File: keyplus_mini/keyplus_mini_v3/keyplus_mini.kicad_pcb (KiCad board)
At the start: 2 copper layers, 24.1 x 23 mm, 23 parts, among them J1 USB_C_Receptacle, J2 Conn_02x09_Odd_Even, J3 CONN_01X01, J4 Conn_02x09_Odd_Even, U1 MCP1700-3302E_SOT23, U2 ATXMEGA-A4U-EPAD

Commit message: cleanup keyplus mini_v3
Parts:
- removed OSHW_Logo: G***, logo:OSHW_3x3mm_SilkS
- added ?: REF**, logo:key+_5mm, F.Cu at (203.2, 114.5)
- added ?: , logo:OSHW_3x3mm_SilkS, B.Cu at (207.1, 112.4)
- C2: footprint Capacitor_SMD:C_1206_3216Metric -> Capacitor_SMD:C_0805_2012Metric
- J1: footprint conn_usb:USB_TypeC_239FC14-00276T-H -> conn_usb:USB_TypeC_Hirose_CX70M-24P1
- moved R3 1.82 mm to (200.8, 98.3)
- moved R1 1.14 mm to (209.6, 102.5), turned to 0 degrees
- moved R5 1.00 mm to (211.8, 102.5)
- moved J1 1.00 mm to (208.0, 92.0)
- moved R4 1.00 mm to (214.1, 102.5)
- moved C2 0.59 mm to (212.7, 104.0)
- moved R2 0.56 mm to (206.3, 102.7), turned to 0 degrees
- moved ? 0.41 mm to (217.1, 95.4)
- moved ? 0.40 mm to (198.9, 95.4)
- moved R6 0.22 mm to (204.9, 102.4)
- moved R7 0.15 mm to (205.3, 103.8)
- moved C1 0.14 mm to (202.8, 105.2)
- moved U1 0.13 mm to (202.3, 102.9)
- moved C5 0.12 mm to (206.8, 104.8)
- moved D1 0.08 mm to (202.4, 107.6)
- renumbered REF** to ?
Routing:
- net +5V: track 16.7 -> 27.3 mm
- net GND: track 25.2 -> 30.4 mm, vias 24 -> 23
- net +3V3: track 82.2 -> 86.3 mm
- net Net-(J1-PadB5): track 2.68 -> 5.51 mm, vias 0 -> 1
- net /PCL: track 16.8 -> 18.6 mm
- net /PE1: track 17.5 -> 19.1 mm
- net /PC2: track 9.31 -> 7.81 mm
- net /D-: track 7.93 -> 9.04 mm, vias 0 -> 1
- net /PA5: track 9.44 -> 10.2 mm
- net Net-(R6-Pad2): track 4.24 -> 4.94 mm
- net /PE0: track 15.6 -> 15.0 mm
- net Net-(C1-Pad2): track 2.61 -> 3.13 mm
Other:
- board size 24.1 x 23 mm -> 24 x 23 mm
- net class 5v removed
- net class Default: via_dia 0.5 -> 0.6
- net class Power added: clearance 0.1524, trace_width 0.25, via_dia 0.6, via_drill 0.3
- net class temp: via_dia 0.5 -> 0.6
- rule trace_min: 0.127 -> 0.1524
- rule via_min_drill: 0.2032 -> 0.3
- rule via_min_size: 0.4572 -> 0.6
- board text added: "keyplus mini"
- board text added: "©jem"
- board text removed: "SPI"

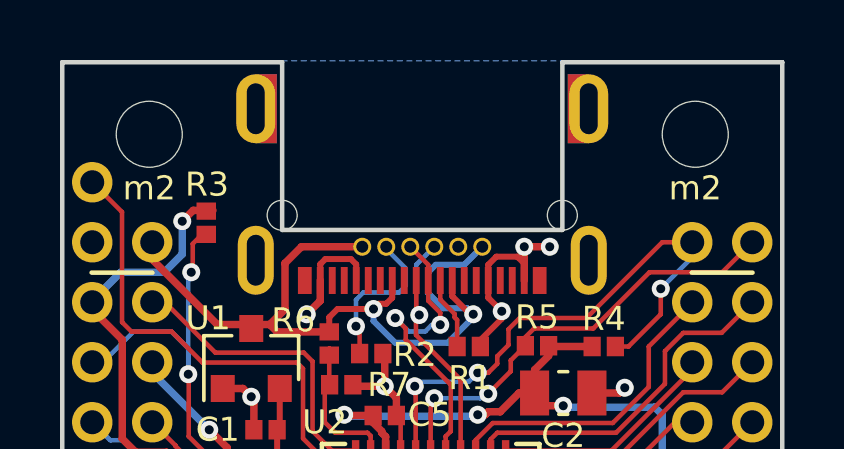
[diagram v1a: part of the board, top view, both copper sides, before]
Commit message: minor PCB fixes and BOM updates
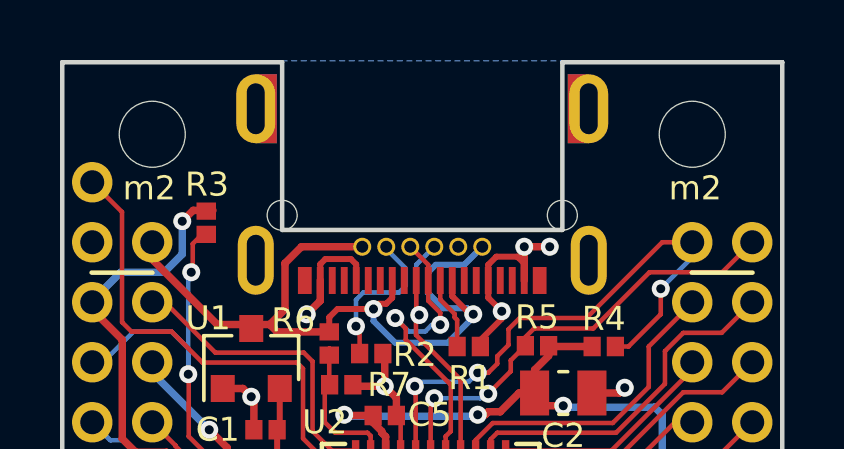
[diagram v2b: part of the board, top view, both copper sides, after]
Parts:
- moved ? 0.10 mm to (199.0, 95.4)
- moved ? 0.10 mm to (217.0, 95.4)
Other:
- rule pad_to_mask_clearance: 0.0381 -> 0.02
- rule solder_mask_min_width: 0.0508 -> 0.05

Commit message: update keyplus mini files for v3
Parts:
- U2: footprint qfn:QFN-44-1EP_7x7mm_Pitch0.5mm_Alt_Silk -> qfn:QFN-44-1EP_7x7mm_Pitch0.5mm
- moved C3 217.4 mm to (17.1, 15.5), turned to 90 degrees
- moved C4 217.1 mm to (13.8, 21.1)
- moved ? 216.9 mm to (3.00, 2.40)
- moved ? 216.9 mm to (21.0, 2.40)
- moved ? 216.9 mm to (7.25, 21.4)
- moved ? 216.9 mm to (11.1, 19.4)
- moved C1 216.9 mm to (6.78, 12.2)
- moved C2 216.9 mm to (16.7, 11.0)
- moved C5 216.9 mm to (10.8, 11.8)
- moved D1 216.9 mm to (6.45, 14.6)
- moved J2 216.9 mm to (1.00, 6.00)
- moved J3 216.9 mm to (1.00, 4.00)
- moved J4 216.9 mm to (21.0, 6.00)
- moved R1 216.9 mm to (13.6, 9.47)
- moved R2 216.9 mm to (10.3, 9.71)
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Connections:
- J1 pad S1: Net-(J1-PadS1) -> (no net)
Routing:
- net +3V3: track 86.3 -> 70.2 mm, vias 7 -> 8
- net +5V: track 27.3 -> 24.3 mm
- net GND: track 30.4 -> 32.8 mm
- net Net-(J1-PadB5): track 5.51 -> 4.28 mm
- net /D+: track 10.1 -> 8.97 mm, vias 2 -> 1
- net /PCL: track 18.6 -> 17.9 mm
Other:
- net class Default: via_drill 0.3 -> 0.4
- net class Power: via_drill 0.3 -> 0.4
- net class temp: via_drill 0.3 -> 0.4
- rule via_min_drill: 0.3 -> 0.4
- board text added: "I2C"
- board text added: "SPI"
